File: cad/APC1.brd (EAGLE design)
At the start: 75.9 x 73.7 mm, 27 parts, among them IC1 LM555N, IC2 LM555N

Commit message: Fixed wiring on pots; more careful routing I had changed the schematic for two pots incorrectly, volume and pulse width. Added two current-limiting resistors for the freq. and pulse width pots. Spent more time with the trace routing. Eliminated a few vias. Widened trace widths and spread out traces to enable (at least potentially) desktop CNC PCB routing, such as with an OtherMill Pro. Changed some of the documentation and many of the images too, naturally. Also changed the .gitignore file to reflect more careful cataloging of the important parts of the project.
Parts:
- added R6, R7: 220R, rcl:0207/7
- moved C2 16.6 mm to (40.9, 5.03), turned to 90 degrees
- moved C4 0.51 mm to (68.1, 37.5)
- turned TOUCHPAD1 to 180 degrees
- turned TOUCHPAD2 to 180 degrees
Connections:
- new net N$13: LINE.1, MOD.2, R5.OUT, R5.WIPE
- new net N$15: R3.IN, R6.2, TOUCHPAD1.1
- net N$1: now also R3.OUT
- net N$14: now also R4.IN, R7.2, TOUCHPAD2.1; no longer LINE.1, MOD.2, R5.OUT
- net N$16: now also R5.IN; no longer R5.WIPE
- net N$3: now also R4.WIPE
- net VCC: now also R6.1, R7.1; no longer R3.IN, R4.WIPE, TOUCHPAD1.1, TOUCHPAD2.1
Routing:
- net N$13: track 0.00 -> 45.1 mm
- net N$14: track 47.5 -> 9.82 mm
- net VCC: track 169.8 -> 134.2 mm, vias 1 -> 0
- net N$15: track 0.00 -> 15.0 mm
- net N$16: track 40.0 -> 52.9 mm
- net N$2: track 17.5 -> 7.21 mm
- net N$4: track 22.3 -> 30.3 mm
- net N$12: track 42.5 -> 46.2 mm
- net N$3: track 57.3 -> 54.4 mm
- net N$1: track 53.7 -> 56.3 mm, vias 1 -> 0
- net N$8: track 19.0 -> 20.7 mm
- net N$9: track 42.9 -> 44.7 mm
- net N$5: track 26.6 -> 25.2 mm
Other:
- board text added: "``Atari Punk Console'' by Forrest Mims III (1980 and 1984; called a `Stepped Tone Generator'). This layout & mods by N5JHH, 2015--2017. v1.1"
- board text removed: "``Atari Punk Console'' by Forrest Mims III (1980 and 1984; called a `Stepped Tone Generator'). This layout & mods by N5JHH, 2015--2017. v1.0"

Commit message: Cleanup and a few additions. Added PCB photo.
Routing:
- net N$12: track 46.2 -> 45.3 mm

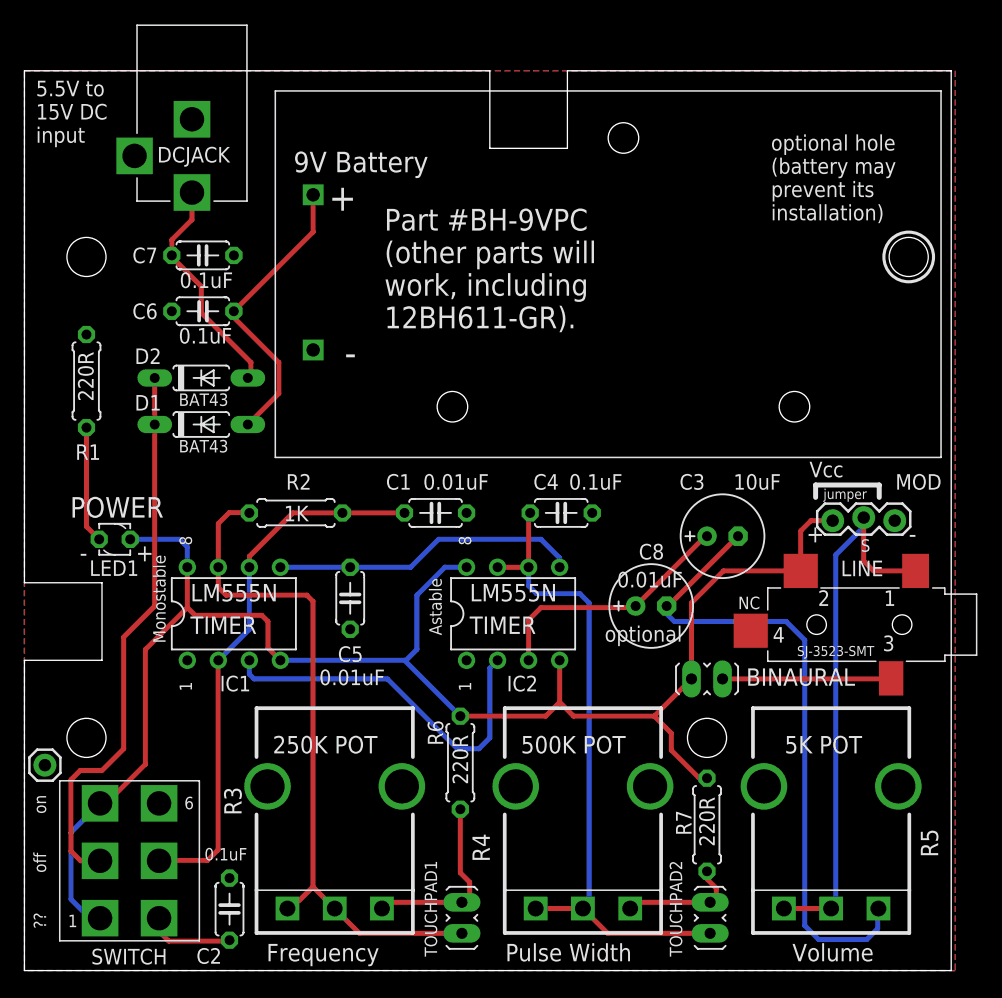
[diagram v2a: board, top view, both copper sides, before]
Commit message: v.1.2 of board. Documentation changes / improvements.
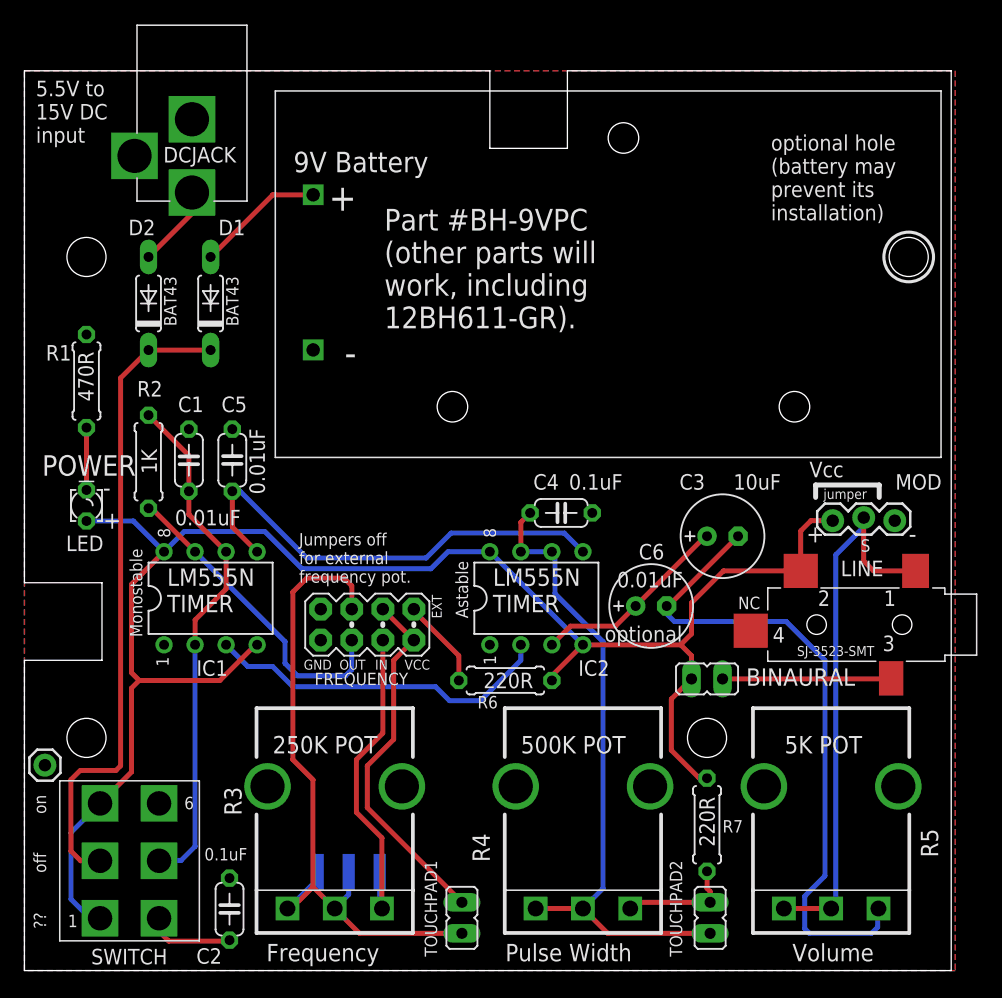
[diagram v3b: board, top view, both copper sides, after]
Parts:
- removed C7: 0.1uF, rcl:C050-024X044
- removed C8: 0.01uF, rcl:E2,5-7
- removed LED1: RED, eagle-ltspice:LED_LD260
- added FREQUENCY: M04X2, SparkFun-Connectors:2X4
- added JP2: FREQ_BYPASS, SparkFun-Connectors:1X03_SMD_RA_MALE
- added LED: RED, eagle-ltspice:LED_LD260
- C6: value 0.1uF -> 0.01uF; device rcl:C050-024X044 -> rcl:E2,5-7
- R1: value 220R -> 470R
- moved C6 43.9 mm to (75.4, 29.8)
- moved C1 20.6 mm to (37.6, 41.8), turned to 270 degrees
- moved C5 14.9 mm to (41.1, 41.8), turned to 90 degrees
- moved R2 12.8 mm to (34.3, 41.7), turned to 90 degrees
- moved D1 9.94 mm to (39.4, 54.6), turned to 90 degrees
- moved R6 7.67 mm to (63.5, 23.7), turned to 180 degrees
- moved D2 7.47 mm to (34.3, 54.6), turned to 90 degrees
- moved IC1 2.29 mm to (39.4, 30.5)
- moved IC2 2.29 mm to (66.0, 30.5)
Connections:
- net N$12 renamed VIN
- new net N$18: FREQUENCY.1, R6.2
- new net N$19: FREQUENCY.4, JP2.1, R3.IN
- new net N$20: FREQUENCY.6, IC1.7, R2.1
- net GND: now also FREQUENCY.7, FREQUENCY.8; no longer C6.1, C7.1
- net N$1: now also FREQUENCY.5, JP2.2, JP2.3; no longer IC1.7, R2.1
- net N$10: no longer C6.2
- net N$11: no longer C7.2
- net N$15: now also FREQUENCY.2, FREQUENCY.3; no longer R3.IN, R6.2
- net N$16: now also C6.-; no longer C8.-
- net N$6: now also LED.K; no longer LED1.K
- net N$8: now also C6.+; no longer C8.+
- net VCC: now also LED.A; no longer LED1.A
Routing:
- net N$19: track 0.00 -> 26.8 mm
- net N$20: track 0.00 -> 26.0 mm
- net N$15: track 15.0 -> 29.8 mm
- net N$10: track 24.1 -> 10.5 mm
- net N$5: track 25.2 -> 38.2 mm
- net N$11: track 18.6 -> 6.74 mm
- net VIN: track 45.3 -> 53.2 mm
- net N$18: track 0.00 -> 7.37 mm
- net VCC: track 134.0 -> 139.7 mm
- net N$6: track 9.58 -> 5.11 mm
- net N$8: track 20.7 -> 16.6 mm
- net N$9: track 44.7 -> 42.5 mm
- net N$4: track 30.3 -> 28.7 mm
- net N$3: track 54.4 -> 52.8 mm
- net N$16: track 52.9 -> 53.9 mm
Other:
- board text added: "C6 is optional but changes the output a bit. MOD allows for external filters or other inputs. EXTERNAL enables off-board sequencers."
- board text added: "EXT"
- board text added: "GND"
- board text added: "IN"
- board text added: "Jumpers off for external frequency pot."
- board text added: "OUT"
- board text added: "VCC"
- board text added: "`Touchpads' can be as simple as two wires. Skin acts like a variable resistor; changes the tone or frequency output just a bit."
- board text added: "``Atari Punk Console'' by Forrest Mims III (1980 and 1984; called a `Stepped Tone Generator'). This layout & mods by N5JHH, 2015--2017. v1.2"
- board text removed: "C8 is optional but changes the output a bit. MOD allows for external filters or other inputs."
- board text removed: "`Touchpads' can be as simple as two wires. Skin acts like a variable resistor and changes the tone or frequency output."
- board text removed: "``Atari Punk Console'' by Forrest Mims III (1980 and 1984; called a `Stepped Tone Generator'). This layout & mods by N5JHH, 2015--2017. v1.1"
